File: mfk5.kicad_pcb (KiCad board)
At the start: 2 copper layers, 84.5 x 57.2 mm, 18 parts, among them SW1 RST, SW2 COL1_ROW1, SW3 COL2_ROW1, SW4 COL1_ROW2, SW5 COL2_ROW2, SW6 COL1_ROW3, U1 Pro Micro

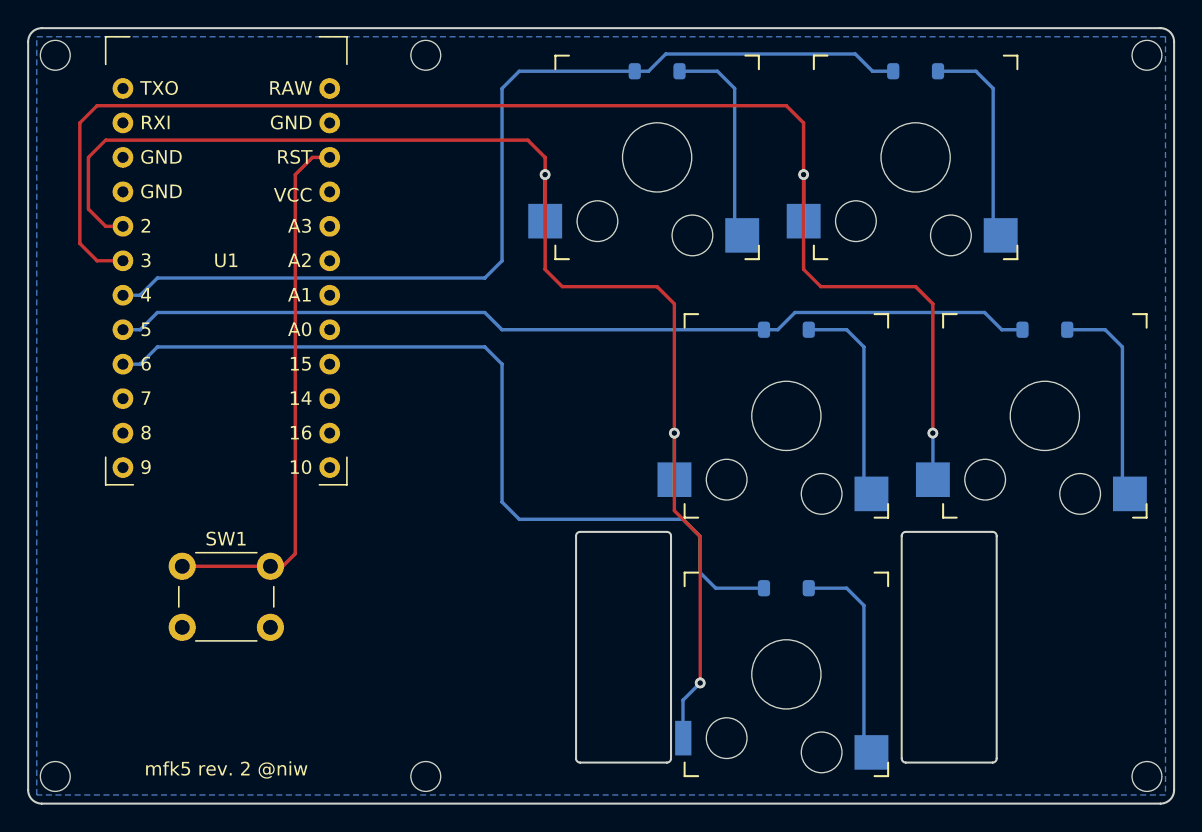
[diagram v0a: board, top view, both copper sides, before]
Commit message: Add ATmega32u4 and related components.
Stop using Pro Micro, going to use PCBA to SMT components.
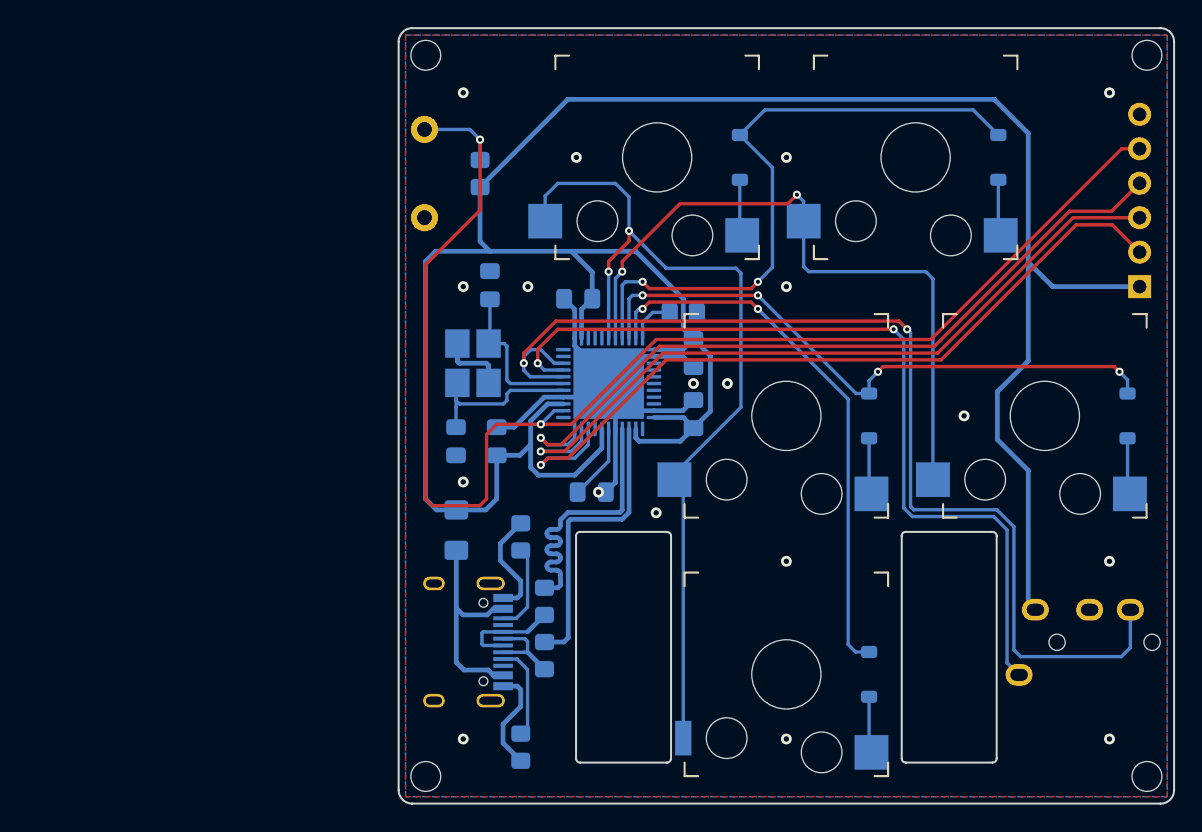
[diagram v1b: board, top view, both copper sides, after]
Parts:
- removed REF** (x2): MountingHole_2.2mm_M2, MountingHole:MountingHole_2.2mm_M2
- added C1: 100n, Capacitor_SMD:C_0805_2012Metric_Pad1.18x1.45mm_HandSolder, B.Cu at (133.1, 106.4)
- added C2: 100n, Capacitor_SMD:C_0805_2012Metric_Pad1.18x1.45mm_HandSolder, B.Cu at (139.1, 95.9)
- added C3: 100n, Capacitor_SMD:C_0805_2012Metric_Pad1.18x1.45mm_HandSolder, B.Cu at (147.6, 99.9)
- added C4: 10u, Capacitor_SMD:C_0805_2012Metric_Pad1.18x1.45mm_HandSolder, B.Cu at (147.6, 104.4)
- added C5: 22p, Capacitor_SMD:C_0805_2012Metric_Pad1.18x1.45mm_HandSolder, B.Cu at (132.6, 94.9)
- added C6: 22p, Capacitor_SMD:C_0805_2012Metric_Pad1.18x1.45mm_HandSolder, B.Cu at (130.1, 106.4)
- added C7: 1u, Capacitor_SMD:C_0805_2012Metric_Pad1.18x1.45mm_HandSolder, B.Cu at (140.1, 110.2)
- added F1: 500m, Fuse:Fuse_1206_3216Metric_Pad1.42x1.75mm_HandSolder, B.Cu at (130.1, 113.0)
- added J1: USB_C_Receptacle_USB2.0, Connector_USB:USB_C_Receptacle_HRO_TYPE-C-31-M-12, B.Cu at (129.5, 121.2)
- added J2: ISP, Connector_PinHeader_2.54mm:PinHeader_1x06_P2.54mm_Vertical, B.Cu at (180.5, 95.0)
- added J3: TRRS Jack, Connector_Additions:TRRS_Jack_3.5mm_PJ320A, B.Cu at (183.0, 121.3)
- added R1: 5.1k, Resistor_SMD:R_0805_2012Metric_Pad1.20x1.40mm_HandSolder, B.Cu at (134.8, 129.0)
- added R2: 5.1k, Resistor_SMD:R_0805_2012Metric_Pad1.20x1.40mm_HandSolder, B.Cu at (134.8, 113.5)
- added R3: 22, Resistor_SMD:R_0805_2012Metric_Pad1.20x1.40mm_HandSolder, B.Cu at (136.6, 122.2)
- added R4: 22, Resistor_SMD:R_0805_2012Metric_Pad1.20x1.40mm_HandSolder, B.Cu at (136.6, 118.2)
- added R5: 10k, Resistor_SMD:R_0805_2012Metric_Pad1.20x1.40mm_HandSolder, B.Cu at (131.8, 86.7)
- added R6: 10k, Resistor_SMD:R_0805_2012Metric_Pad1.20x1.40mm_HandSolder, B.Cu at (146.8, 96.9)
- added Y1: 16M, Crystal:Crystal_SMD_3225-4Pin_3.2x2.5mm_HandSoldering, B.Cu at (131.3, 100.7)
- SW1: footprint Button_Switch_THT:SW_PUSH_6mm -> Button_Switch_Additions:SW_Push_3.5x6mm_THT; moved to B.Cu
- U1: value Pro Micro -> ATmega32U4-M; footprint Pro_Micro:Pro_Micro -> Package_DFN_QFN:QFN-44-1EP_7x7mm_P0.5mm_EP5.2x5.2mm; moved to B.Cu
- moved SW1 34.0 mm to (127.8, 86.7), turned to -90 degrees
- moved U1 29.6 mm to (141.3, 102.2), turned to 90 degrees
- moved D1 8.80 mm to (151.0, 85.5), turned to -90 degrees
- moved D2 8.80 mm to (170.0, 85.5), turned to -90 degrees
- moved D4 8.80 mm to (179.6, 104.6), turned to -90 degrees
- moved D3 8.80 mm to (160.5, 104.6), turned to -90 degrees
- moved D5 8.80 mm to (160.5, 123.6), turned to -90 degrees
- renumbered REF** to MH1, REF** to MH2, REF** to MH3, REF** to MH4
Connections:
- SW1 pad 1: RST -> RESET
- U1 pad 10: unconnected-(U1-7-Pad10) -> MOSI
- U1 pad 11: unconnected-(U1-8-Pad11) -> MISO
- U1 pad 13: unconnected-(U1-10-Pad13) -> RESET
- U1 pad 14: unconnected-(U1-16-Pad14) -> +5V
- U1 pad 15: unconnected-(U1-14-Pad15) -> GND
- U1 pad 16: unconnected-(U1-15-Pad16) -> XTAL2
- U1 pad 17: unconnected-(U1-A0-Pad17) -> XTAL1
- U1 pad 18: unconnected-(U1-A1-Pad18) -> SCL_SERIAL
- U1 pad 19: unconnected-(U1-A2-Pad19) -> SDA
- U1 pad 2: unconnected-(U1-RXI-Pad2) -> +5V
- U1 pad 20: unconnected-(U1-A3-Pad20) -> SCL_SERIAL
- U1 pad 21: +5V -> unconnected-(U1-PD3-Pad21)
- U1 pad 22: RST -> unconnected-(U1-PD5-Pad22)
- U1 pad 24: unconnected-(U1-RAW-Pad24) -> +5V
- U1 pad 3: GND -> USB_D-
- U1 pad 4: GND -> USB_D+
- U1 pad 5: COL1 -> GND
- U1 pad 6: COL2 -> Net-(U1-UCAP)
- U1 pad 7: ROW1 -> +5V
- U1 pad 8: ROW2 -> unconnected-(U1-PB0-Pad8)
- U1 pad 9: ROW3 -> SCLK
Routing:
- net +5V: track 0.00 -> 189.8 mm
- net RESET: track 0.00 -> 102.6 mm, vias 0 -> 2
- net SCL_SERIAL: track 0.00 -> 80.4 mm, vias 0 -> 2
- net SDA: track 0.00 -> 62.8 mm, vias 0 -> 2
- net GND: track 0.00 -> 61.2 mm, vias 0 -> 18
- net SCLK: track 0.00 -> 57.6 mm, vias 0 -> 1
- net MISO: track 0.00 -> 55.9 mm, vias 0 -> 1
- net MOSI: track 0.00 -> 55.5 mm, vias 0 -> 1
- net COL2: track 104.7 -> 51.0 mm
- net RST: track 39.7 -> 0.00 mm
- net COL1: track 100.3 -> 66.0 mm, vias 3 -> 2
- net ROW1: track 72.1 -> 47.3 mm, vias 0 -> 2
- net ROW2: track 68.4 -> 45.5 mm, vias 0 -> 4
- net ROW3: track 62.6 -> 40.7 mm, vias 0 -> 2
- net USB_D-: track 0.00 -> 21.4 mm
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- added copper zone on F.Cu, net GND
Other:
- board size 84.5 x 57.2 mm -> 57.2 x 57.2 mm
- board text added: "+5V"
- board text added: "GND"
- board text added: "MISO"
- board text added: "MOSI"
- board text added: "RESET"
- board text added: "SCLK"
- board text added: "mfk5 rev. 3 @niw"
- board text removed: "mfk5 rev. 2 @niw"
